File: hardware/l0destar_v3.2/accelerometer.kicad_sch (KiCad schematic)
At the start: 7 parts

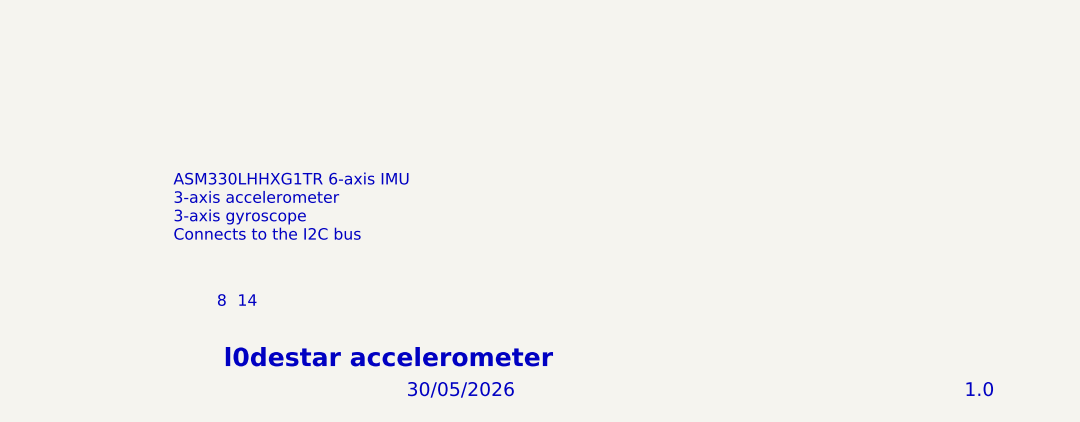
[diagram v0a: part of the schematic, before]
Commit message: update sheet annotations
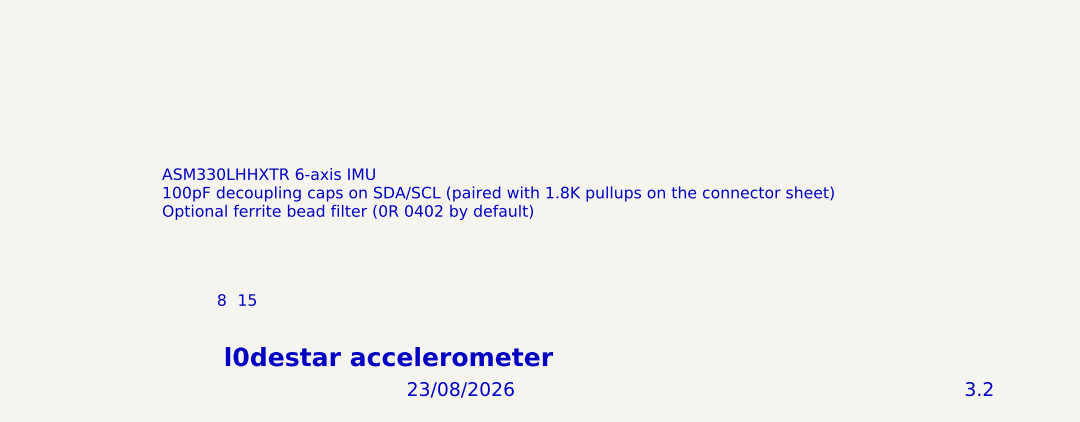
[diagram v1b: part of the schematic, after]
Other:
- note added: "15"
- note added: "23/08/2026"
- note added: "3.2"
- note added: "ASM330LHHXTR 6-axis IMU 100pF decoupling caps on SDA/SCL (paired with 1.8K pullups on the connector sheet) Optional ferrite bead filter (0R 0402 by default)"
- note removed: "1.0"
- note removed: "14"
- note removed: "30/05/2026"
- note removed: "ASM330LHHXG1TR 6-axis IMU 3-axis accelerometer 3-axis gyroscope Connects to the I2C bus"
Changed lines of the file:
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@@
 	(generator_version "10.0")
 	(paper "A4")
-	(text "30/05/2026"
+	(text "23/08/2026"
 		(exclude_from_sim no)
 		(at 206.248 193.294 0)
@@
 		)
 	)
-	(text "ASM330LHHXG1TR 6-axis IMU\n3-axis accelerometer\n3-axis gyroscope\nConnects to the I2C bus"
+	(text "ASM330LHHXTR 6-axis IMU\n100pF decoupling caps on SDA/SCL (paired with 1.8K pullups on the connector sheet)\nOptional ferrite bead filter (0R 0402 by default)"
 		(exclude_from_sim no)
-		(at 180.34 172.974 0)
+		(at 179.07 171.45 0)
 		(effects
 			(font
@@
 		)
 	)
-	(text "1.0"
+	(text "3.2"
 		(exclude_from_sim no)
 		(at 268.224 193.294 0)
@@
 		)
 	)
-	(text "14"
+	(text "15"
 		(exclude_from_sim no)
 		(at 187.452 183.388 0)

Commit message: schematic<>readme discrepency fixes
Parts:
- S8C1, S8C3: value 0402 100nF 10V 10% X7R -> 0402 100nF 50V 10% X7R; Manufacturer_Name Multicomp Pro -> Murata; Manufacturer_Part_Number MC0402B104K250CT -> GRM155R71H104KE14D
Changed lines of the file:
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@@
 			)
 		)
-		(property "Value" "0402 100nF 10V 10% X7R"
+		(property "Value" "0402 100nF 50V 10% X7R"
 			(at 136.906 43.815 0)
 			(show_name no)
@@
 			)
 		)
-		(property "Datasheet" "https://uk.farnell.com/multicomp-pro/mc0402b104k250ct/cap-0-1-f-25v-10-x7r-0402/dp/2320759"
+		(property "Datasheet" ""
 			(at 135.89 37.465 0)
 			(hide yes)
@@
 			)
 		)
-		(property "Description" "Unpolarized capacitor"
+		(property "Description" ""
 			(at 135.89 37.465 0)
 			(hide yes)
@@
 			)
 		)
-		(property "Manufacturer_Part_Number" "MC0402B104K250CT"
+		(property "Manufacturer_Part_Number" "GRM155R71H104KE14D"
 			(at 135.89 37.465 0)
 			(hide yes)
@@
 			)
 		)
-		(property "Manufacturer_Name" "Multicomp Pro"
+		(property "Manufacturer_Name" "Murata"
 			(at 135.89 37.465 0)
 			(hide yes)
@@
 			)
 		)
-		(property "Value" "0402 100nF 10V 10% X7R"
+		(property "Value" "0402 100nF 50V 10% X7R"
 			(at 105.41 37.719 0)
 			(show_name no)
@@
 			)
 		)
-		(property "Datasheet" "https://uk.farnell.com/multicomp-pro/mc0402b104k250ct/cap-0-1-f-25v-10-x7r-0402/dp/2320759"
+		(property "Datasheet" ""
 			(at 101.6 36.195 0)
 			(hide yes)
@@
 			)
 		)
-		(property "Description" "Unpolarized capacitor"
+		(property "Description" ""
 			(at 101.6 36.195 0)
 			(hide yes)
@@
 			)
 		)
-		(property "Manufacturer_Part_Number" "MC0402B104K250CT"
+		(property "Manufacturer_Part_Number" "GRM155R71H104KE14D"
 			(at 101.6 36.195 0)
 			(hide yes)
@@
 			)
 		)
-		(property "Manufacturer_Name" "Multicomp Pro"
+		(property "Manufacturer_Name" "Murata"
 			(at 101.6 36.195 0)
 			(hide yes)
